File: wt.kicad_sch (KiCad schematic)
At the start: 12 parts, among them U1 STM32F407VGTx

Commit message: working on the schema
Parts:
- added D?: USR2, symbol Device:LED
- added D?: w01, symbol Device:LED
- added D?: USR1, symbol Device:LED
- added D?: W02, symbol Device:LED
- added D?: W15, symbol Device:LED
- added D?: W17, symbol Device:LED
- added D?: W03, symbol Device:LED
- added D?: W06, symbol Device:LED
- added D?: W05, symbol Device:LED
- added D?: W12, symbol Device:LED
- added D?: W11, symbol Device:LED
- added D?: W16, symbol Device:LED
- added D?: W00, symbol Device:LED
- added D?: W07, symbol Device:LED
- added D?: W10, symbol Device:LED
- added D?: W14, symbol Device:LED
- added D?: W04, symbol Device:LED
- added D?: W13, symbol Device:LED
- added Out_2: LUM-1502-03_3.5mm_mono_vertical_jack, eurorack:LUM 1502-03, symbol eurorack:LUM-1502-03_3.5mm_mono_vertical_jack
- added R? (x18): R-330-1206, Resistor_SMD:R_1206_3216Metric_Pad1.30x1.75mm_HandSolder, symbol eurorack:R-330-1206
- gave numbers to parts that had none: 2
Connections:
- net GND: now also Out_1.S, D?.1 (K), D?.1 (K), D?.1 (K), D?.1 (K), D?.1 (K), D?.1 (K), D?.1 (K), D?.1 (K), D?.1 (K), D?.1 (K), D?.1 (K), D?.1 (K), D?.1 (K), D?.1 (K), D?.1 (K), D?.1 (K), D?.1 (K), D?.1 (K), Out_2.S
- net Mix/In1: now also Out_1.T, Out_1.TN
- net Mix/In2: now also Out_2.T, Out_2.TN
- net at U1.1 (PE2): now also R?.2
- net at U1.12 (PH0): now also R?.2
- net at U1.13 (PH1): now also R?.2
- net BTN_USR1/Btn: now reaches U1.17 (PC2)
- net BTN_USR2/Btn: now reaches U1.18 (PC3)
- net at U1.2 (PE3): now also R?.2
- net at U1.3 (PE4): now also R?.2
- net at U1.38 (PE7): now also R?.2
- net at U1.39 (PE8): now also R?.2
- net at U1.4 (PE5): now also R?.2
- net at U1.40 (PE9): now also R?.2
- net at U1.41 (PE10): now also R?.2
- net at U1.42 (PE11): now also R?.2
- net at U1.43 (PE12): now also R?.2
- net at U1.44 (PE13): now also R?.2
- net at U1.45 (PE14): now also R?.2
- net at U1.46 (PE15): now also R?.2
- net at U1.5 (PE6): now also R?.2
- net BTN_EDT1/Btn: now reaches U1.63 (PC6)
- net BTN_EDT2/Btn: now reaches U1.64 (PC7)
- net at U1.97 (PE0): now also R?.2
- net at U1.98 (PE1): now also R?.2
- new net: D?.2 (A), R?.1 (x18)
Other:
- sheet Pot CH1-A1 renamed Pot CH1-A
- sheet Pot CH1-D1 renamed Pot CH1-D
- sheet Pot CH1-R1 renamed Pot CH1-R
- sheet Pot CH1-S1 renamed Pot CH1-S
- added sheet BTN_EDT1 (button.kicad_sch)
- added sheet BTN_EDT2 (button.kicad_sch)
- added sheet BTN_USR1 (button.kicad_sch)
- added sheet BTN_USR2 (button.kicad_sch)
- moved on the sheet: Out_1

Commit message: started to work on power part
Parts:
- D1, D10, D11, D12, D13, D14, D15, D16, D17, D18, D2, D3, D4, D5, D6, D7, D8, D9: renamed from D?; footprint (none) -> Diode_SMD:D_1206_3216Metric_Pad1.42x1.75mm_HandSolder
- gave numbers to parts that had none: 27
- renumbered Out_Mix to Out_Mix1, U1 to U2
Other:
- added sheet Power (power.kicad_sch)

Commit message: working on powers
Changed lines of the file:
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@@
     )
   )
-  (sheet (at 20.955 20.32) (size 20.955 22.225) (fields_autoplaced)
+  (sheet (at 20.955 20.32) (size 12.7 3.81) (fields_autoplaced)
     (stroke (width 0.1524) (type solid) (color 0 0 0 0))
     (fill (color 0 0 0 0.0000))
@@
       (effects (font (size 1.27 1.27)) (justify left bottom))
     )
-    (property "Sheet file" "power.kicad_sch" (id 1) (at 20.955 43.1296 0)
+    (property "Sheet file" "power.kicad_sch" (id 1) (at 20.955 24.7146 0)
       (effects (font (size 1.27 1.27)) (justify left top))
     )
@@
       (reference "#PWR060") (unit 1) (value "GND") (footprint "")
     )
+    (path "/e824c659-32ba-400c-8fa0-3368d4abf8c1/c5fc2c58-21e2-4f25-8c8f-aa3e34314e8b"
+      (reference "#PWR061") (unit 1) (value "+12V") (footprint "")
+    )
+    (path "/e824c659-32ba-400c-8fa0-3368d4abf8c1/d70df1d4-55f1-4a69-b683-20b792952e85"
+      (reference "#PWR062") (unit 1) (value "-12V") (footprint "")
+    )
+    (path "/e824c659-32ba-400c-8fa0-3368d4abf8c1/937895b2-5ca8-4752-94c7-d0c154a59ebf"
+      (reference "#PWR063") (unit 1) (value "GND") (footprint "")
+    )
     (path "/e824c659-32ba-400c-8fa0-3368d4abf8c1/096b5392-b9dc-427a-8737-ea092f5d8dc6"
-      (reference "#PWR?") (unit 1) (value "+12V") (footprint "")
+      (reference "#PWR064") (unit 1) (value "+12V") (footprint "")
+    )
+    (path "/e824c659-32ba-400c-8fa0-3368d4abf8c1/2df66250-7ab7-47d2-9e26-c353fdeb0a68"
+      (reference "#PWR065") (unit 1) (value "+5V") (footprint "")
     )
     (path "/e824c659-32ba-400c-8fa0-3368d4abf8c1/866bfefe-2ba6-43d6-bdb5-9bfb4adf7a60"
-      (reference "#PWR?") (unit 1) (value "+5V") (footprint "")
-    )
-    (path "/e824c659-32ba-400c-8fa0-3368d4abf8c1/937895b2-5ca8-4752-94c7-d0c154a59ebf"
-      (reference "#PWR?") (unit 1) (value "GND") (footprint "")
+      (reference "#PWR066") (unit 1) (value "+5V") (footprint "")
     )
     (path "/e824c659-32ba-400c-8fa0-3368d4abf8c1/a5a2614f-46c7-49b5-8808-5926f2cce3af"
-      (reference "#PWR?") (unit 1) (value "GND") (footprint "")
-    )
-    (path "/e824c659-32ba-400c-8fa0-3368d4abf8c1/c5fc2c58-21e2-4f25-8c8f-aa3e34314e8b"
-      (reference "#PWR?") (unit 1) (value "+12V") (footprint "")
-    )
-    (path "/e824c659-32ba-400c-8fa0-3368d4abf8c1/d70df1d4-55f1-4a69-b683-20b792952e85"
-      (reference "#PWR?") (unit 1) (value "-12V") (footprint "")
+      (reference "#PWR067") (unit 1) (value "GND") (footprint "")
+    )
+    (path "/e824c659-32ba-400c-8fa0-3368d4abf8c1/8c462594-9baf-4f21-b294-2cb5f3c49694"
+      (reference "#PWR068") (unit 1) (value "+3V3") (footprint "")
+    )
+    (path "/e824c659-32ba-400c-8fa0-3368d4abf8c1/0cd7cf84-f35d-4b56-b015-61b7817bc01f"
+      (reference "#PWR069") (unit 1) (value "GND") (footprint "")
+    )
+    (path "/e824c659-32ba-400c-8fa0-3368d4abf8c1/0671fe2c-4d2a-4ddb-849f-9250cbc0774a"
+      (reference "#PWR070") (unit 1) (value "-12V") (footprint "")
+    )
+    (path "/e824c659-32ba-400c-8fa0-3368d4abf8c1/b217e4a1-72f2-441d-b0dd-72b955caee1d"
+      (reference "#PWR071") (unit 1) (value "GND") (footprint "")
+    )
+    (path "/e824c659-32ba-400c-8fa0-3368d4abf8c1/c6c35c50-ee92-482c-822b-b0ac9f326d33"
+      (reference "#PWR072") (unit 1) (value "GND") (footprint "")
+    )
+    (path "/e824c659-32ba-400c-8fa0-3368d4abf8c1/d894002e-b1bf-4713-90cb-8080a2caa4b2"
+      (reference "#PWR073") (unit 1) (value "-1V65") (footprint "")
+    )
+    (path "/e824c659-32ba-400c-8fa0-3368d4abf8c1/b10e15b9-40be-4b1f-a8b3-096805b626e7"
+      (reference "#PWR074") (unit 1) (value "+12V") (footprint "")
+    )
+    (path "/e824c659-32ba-400c-8fa0-3368d4abf8c1/4684409c-a186-48aa-a9a1-4ff36a8a81e4"
+      (reference "#PWR075") (unit 1) (value "-12V") (footprint "")
     )
     (path "/621d9a5d-8d47-42eb-9672-3a0d6fc71e93"
@@
       (reference "C14") (unit 1) (value "C-100nF-0805") (footprint "Capacitor_SMD:C_0805_2012Metric_Pad1.18x1.45mm_HandSolder")
     )
+    (path "/e824c659-32ba-400c-8fa0-3368d4abf8c1/99244614-7540-475b-86fe-438116ab29e4"
+      (reference "C15") (unit 1) (value "C-Pol-10uF-TAN") (footprint "Capacitor_Tantalum_SMD:CP_EIA-6032-28_Kemet-C")
+    )
     (path "/e824c659-32ba-400c-8fa0-3368d4abf8c1/469ff368-5ab8-471a-93d7-0000342f848d"
-      (reference "C?") (unit 1) (value "C-Pol-10uF-TAN") (footprint "Capacitor_Tantalum_SMD:CP_EIA-6032-28_Kemet-C")
-    )
-    (path "/e824c659-32ba-400c-8fa0-3368d4abf8c1/99244614-7540-475b-86fe-438116ab29e4"
-      (reference "C?") (unit 1) (value "C-Pol-10uF-TAN") (footprint "Capacitor_Tantalum_SMD:CP_EIA-6032-28_Kemet-C")
+      (reference "C16") (unit 1) (value "C-Pol-10uF-TAN") (footprint "Capacitor_Tantalum_SMD:CP_EIA-6032-28_Kemet-C")
+    )
+    (path "/e824c659-32ba-400c-8fa0-3368d4abf8c1/a2eb37e4-dc46-4823-b91e-901dae674c2b"
+      (reference "C17") (unit 1) (value "C-Pol-10uF-TAN") (footprint "Capacitor_Tantalum_SMD:CP_EIA-6032-28_Kemet-C")
     )
     (path "/30425711-eeee-4f77-98cd-942ad6c950a9"
@@
       (reference "RV10") (unit 1) (value "Pot_500") (footprint "Potentiometer_THT:Potentiometer_Piher_PT-10-V10_Vertical")
     )
+    (path "/e824c659-32ba-400c-8fa0-3368d4abf8c1/198d0af1-5b67-4603-95c5-4cd87c500db2"
+      (reference "RV11") (unit 1) (value "Trim_5k_prec_tht") (footprint "eurorack:trim_2.5mm")
+    )
     (path "/91e74aa6-705f-40ba-b6bd-d9322523111d/6146eab9-fca2-4bb4-bc11-0a211214f1c3"
       (reference "SW1") (unit 1) (value "SW_Push") (footprint "Button_Switch_SMD:SW_Push_1P1T_NO_6x6mm_H9.5mm")
@@
     )
     (path "/e824c659-32ba-400c-8fa0-3368d4abf8c1/0110dc09-7260-4b72-824b-88272648f7c3"
-      (reference "U?") (unit 1) (value "power_conn_10") (footprint "eurorack:power_10")
+      (reference "U7") (unit 1) (value "power_conn_10") (footprint "eurorack:power_10")
     )
     (path "/e824c659-32ba-400c-8fa0-3368d4abf8c1/4698fe25-be48-4bd9-9c3f-bff9cceafc29"
-      (reference "U?") (unit 1) (value "L78L05ACU") (footprint "Package_TO_SOT_SMD:SOT-89-3_Handsoldering")
+      (reference "U8") (unit 1) (value "L78L05ACU") (footprint "Package_TO_SOT_SMD:SOT-89-3_Handsoldering")
+    )
+    (path "/e824c659-32ba-400c-8fa0-3368d4abf8c1/885721f2-5906-4c87-b7c5-9a9ae02f9855"
+      (reference "U9") (unit 1) (value "ZLDO1117G33TA") (footprint "Package_TO_SOT_SMD:SOT-223")
+    )
+    (path "/e824c659-32ba-400c-8fa0-3368d4abf8c1/80d37fb5-8049-4042-a6cf-7f4a87fb0437"
+      (reference "U10") (unit 1) (value "TL072") (footprint "Package_SO:SO-8_3.9x4.9mm_P1.27mm")
+    )
+    (path "/e824c659-32ba-400c-8fa0-3368d4abf8c1/a158265f-a889-4167-b823-8e329fdd6be2"
+      (reference "U10") (unit 2) (value "TL072") (footprint "Package_SO:SO-8_3.9x4.9mm_P1.27mm")
+    )
+    (path "/e824c659-32ba-400c-8fa0-3368d4abf8c1/d7c6bc66-4df3-4b71-886c-32c400735cc3"
+      (reference "U10") (unit 3) (value "TL072") (footprint "Package_SO:SO-8_3.9x4.9mm_P1.27mm")
     )
   )

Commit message: WIP
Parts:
- removed C1, C4: C-100nF-0805, Capacitor_SMD:C_0805_2012Metric_Pad1.18x1.45mm_HandSolder, symbol eurorack:C-100nF-0805
- removed C2: C-Pol-10uF-FK-V, Capacitor_SMD:CP_Elec_8x6.2, symbol eurorack:C-Pol-10uF-FK-V
- removed C3: C-Pol-1uF-FK-V, Capacitor_SMD:C_1206_3216Metric, symbol eurorack:C-Pol-1uF-FK-V
- removed U1: REF191, Package_SO:SO-8_3.9x4.9mm_P1.27mm, symbol eurorack:REF191
- added C?: C-100nF-0805, Capacitor_SMD:C_0805_2012Metric_Pad1.18x1.45mm_HandSolder, symbol eurorack:C-100nF-0805
- added R? (x2): R-100k-0603, Resistor_SMD:R_0603_1608Metric, symbol eurorack:R-100k-0603
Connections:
- net +3V3: now also U2.6 (VBAT), R?.1
- net GND: now also C?.2, R?.1
- net at U2.14 (NRST): now also C?.1, R?.2
- net at U2.94 (BOOT0): now also R?.2

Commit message: WIP
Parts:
- added C? (x2): C-2u2-1812, Capacitor_SMD:C_1812_4532Metric_Pad1.57x3.40mm_HandSolder, symbol eurorack:C-2u2-1812
- added C? (x2): C-22pF-0805, Capacitor_SMD:C_0805_2012Metric_Pad1.18x1.45mm_HandSolder, symbol eurorack:C-22pF-0805
- added R?: R-220-1206, Resistor_SMD:R_1206_3216Metric_Pad1.30x1.75mm_HandSolder, symbol eurorack:R-220-1206
- added Y?: Crystal_8Mhz, eurorack:HC49-4HSMX, symbol eurorack:Crystal_8Mhz
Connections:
- net GND: now also C?.2, C?.2, C?.2, C?.2
- net at R1.2: now also U2.77 (PA15); no longer U2.12 (PH0)
- net at U2.13 (PH1): now also R?.2; no longer R2.2
- net at U2.49 (VCAP_1): now also C?.1
- net at U2.73 (VCAP_2): now also C?.1
- net at U2.76 (PA14): now also R2.2
- new net: C?.1, U2.12 (PH0), Y?.2
- new net: C?.1, R?.1, Y?.1
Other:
- moved on the sheet: D1, D2, R1, R2

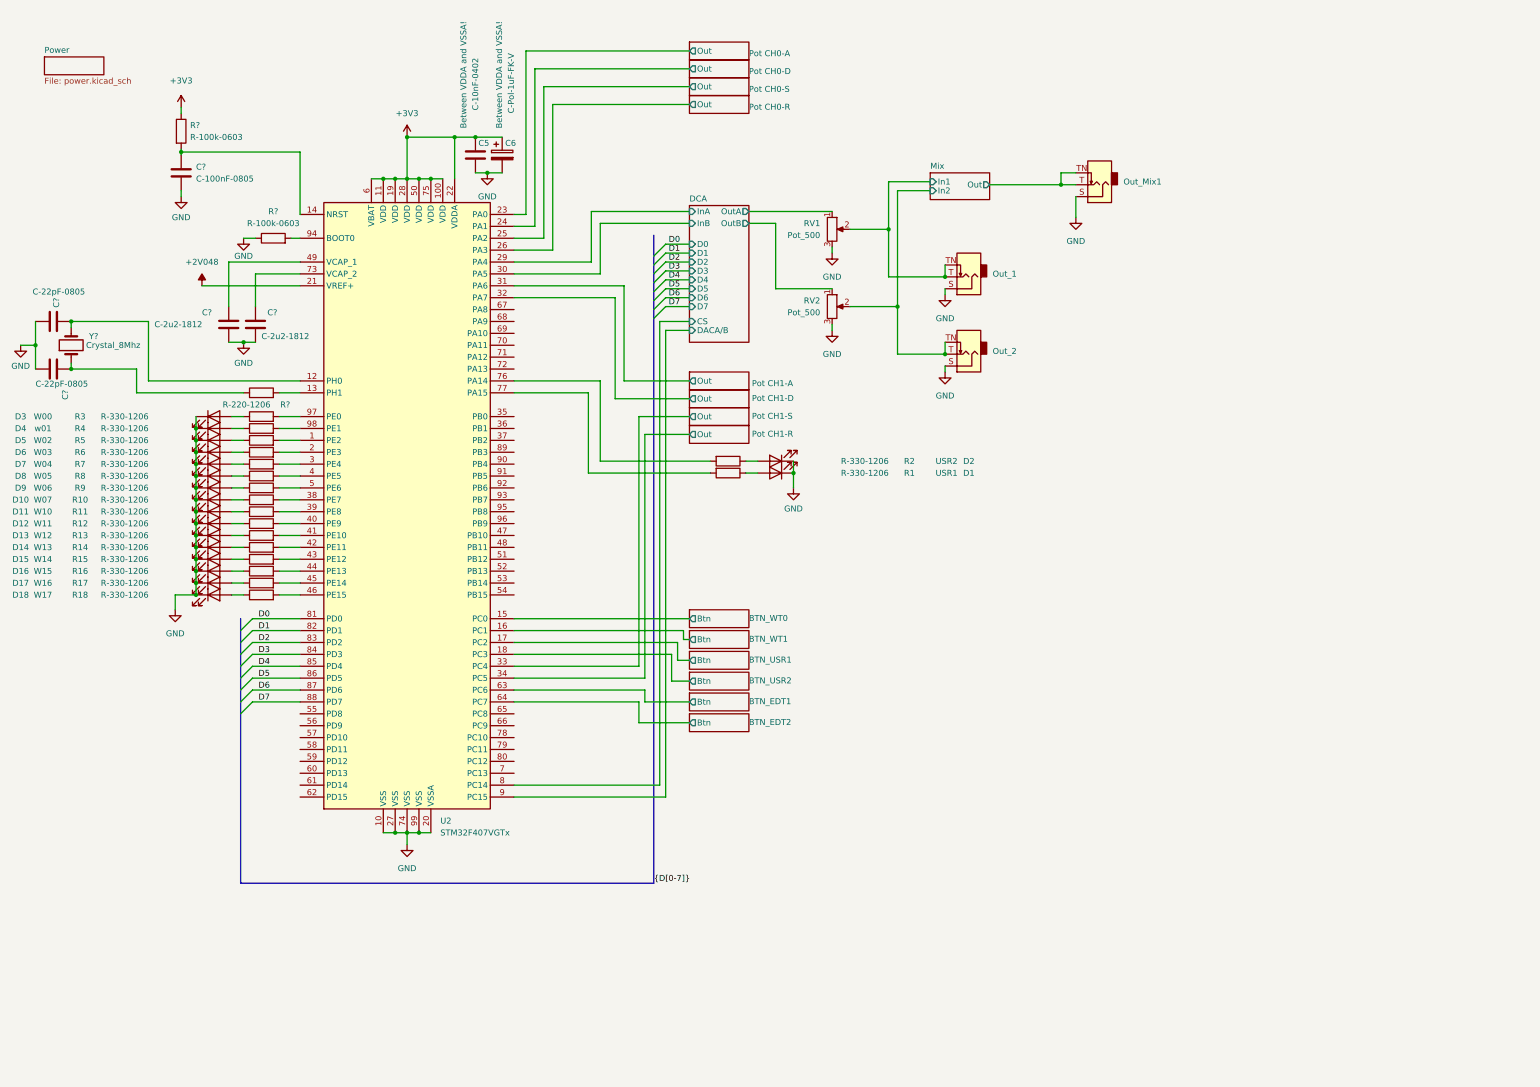
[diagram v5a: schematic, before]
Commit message: refactoring with global labels
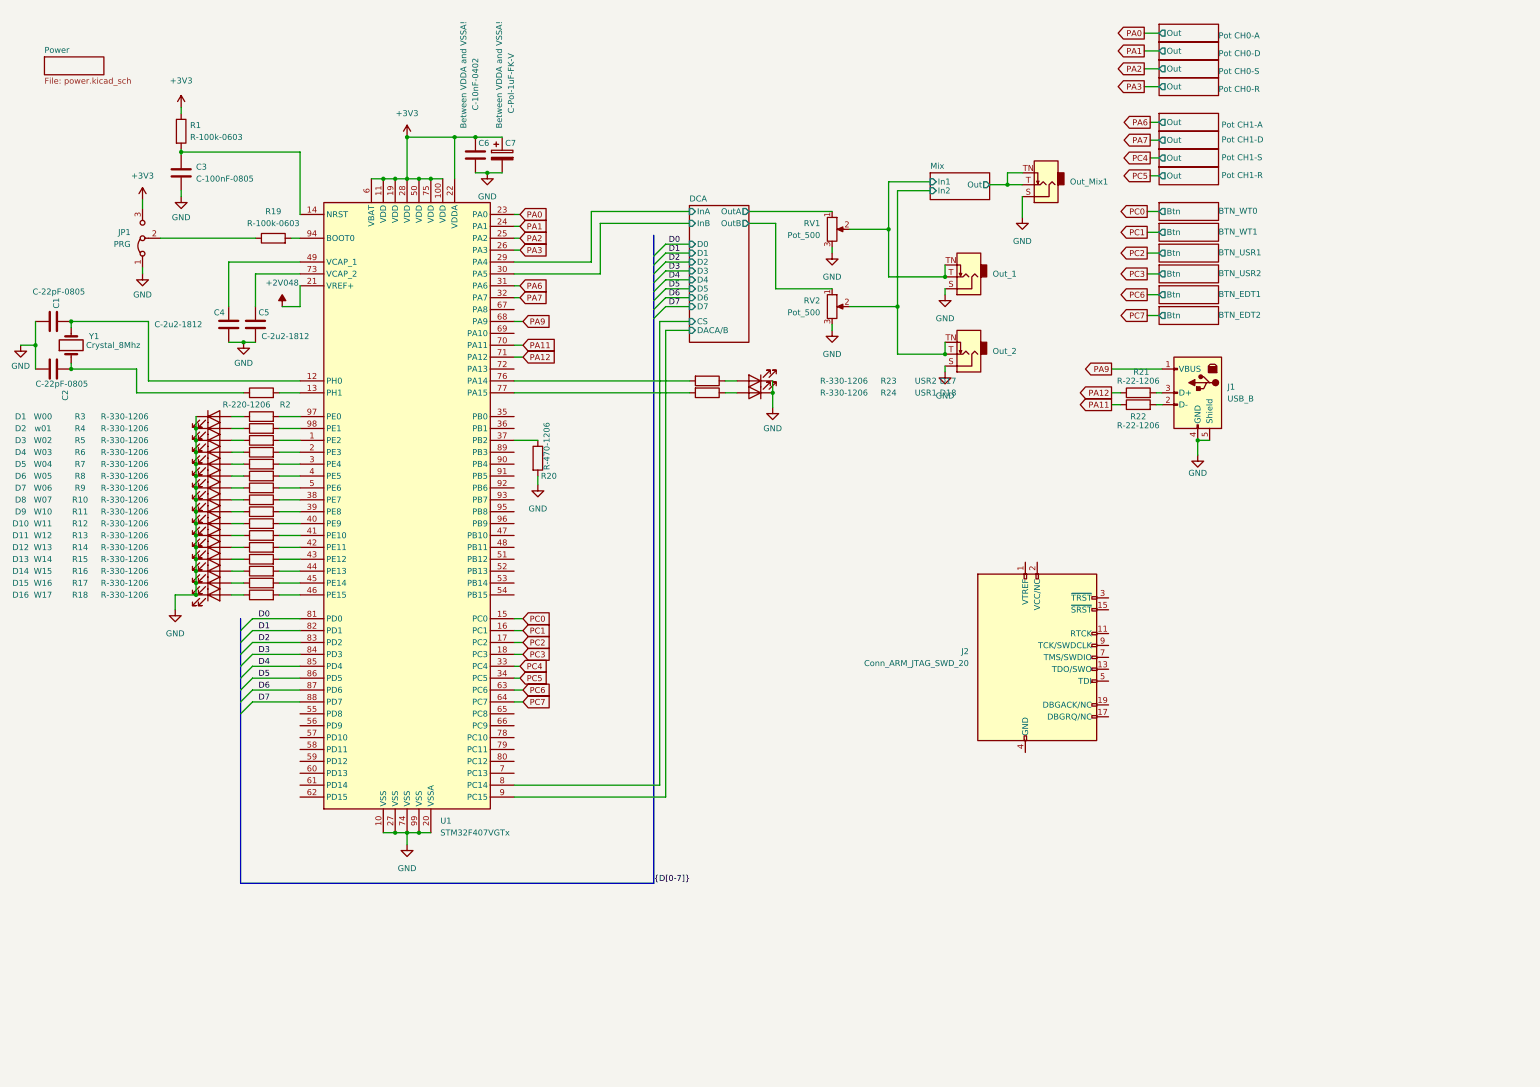
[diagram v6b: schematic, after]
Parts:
- added J1: USB_B, eurorack:USB-BG, symbol eurorack:USB_B
- added J2: Conn_ARM_JTAG_SWD_20, symbol Connector:Conn_ARM_JTAG_SWD_20
- added JP1: PRG, symbol Jumper:Jumper_3_Bridged12
- added R20: R-470-1206, Resistor_SMD:R_1206_3216Metric_Pad1.30x1.75mm_HandSolder, symbol eurorack:R-470-1206
- added R21, R22: R-22-1206, Resistor_SMD:R_1206_3216Metric_Pad1.30x1.75mm_HandSolder, symbol eurorack:R-22-1206
- gave numbers to parts that had none: 9
- renumbered C5 to C6, C6 to C7, D3 to D1, D12 to D10, D13 to D11, D14 to D12, D15 to D13, D16 to D14, D17 to D15, D18 to D16, D2 to D17, D1 to D18, D4 to D2, D5 to D3, D6 to D4, D7 to D5, D8 to D6, D9 to D7, D10 to D8, D11 to D9, R2 to R23, R1 to R24, U2 to U1
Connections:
- net +3V3: now also JP1.3 (B)
- net GND: now also J1.4 (GND), J1.5 (Shield), JP1.1 (A), R20.2; no longer R19.1
- net at U1.37 (PB2): now also R20.1
- net PA9: now reaches U1.68 (PA9)
- net PA9: now also J1.1 (VBUS)
- net PA11: now reaches U1.70 (PA11)
- net PA11: now also R22.1
- net PA12: now reaches U1.71 (PA12)
- net PA12: now also R21.1
- net BTN_EDT1/Btn renamed PC6
- net BTN_EDT2/Btn renamed PC7
- net BTN_USR1/Btn renamed PC2
- net BTN_USR2/Btn renamed PC3
- net BTN_WT0/Btn renamed PC0
- net BTN_WT1/Btn renamed PC1
- net Pot CH0-A/Out renamed PA0
- net Pot CH0-D/Out renamed PA1
- net Pot CH0-R/Out renamed PA3
- net Pot CH0-S/Out renamed PA2
- net Pot CH1-A/Out renamed PA6
- net Pot CH1-D/Out renamed PA7
- net Pot CH1-R/Out renamed PC5
- net Pot CH1-S/Out renamed PC4
- new net: JP1.2 (C), R19.1
- new net: J1.2 (D-), R22.2
- new net: J1.3 (D+), R21.2
- new net: J2.10 (GND), J2.12 (GND), J2.14 (GND), J2.16 (GND), J2.18 (GND), J2.20 (GND), J2.4 (GND), J2.6 (GND), J2.8 (GND)
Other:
- moved on the sheet: D17, D18, Out_Mix1, R23, R24
